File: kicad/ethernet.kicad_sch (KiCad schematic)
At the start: 83 parts, among them J1 RJ45_Abracon_ARJP11A-MASA-B-A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, J2 Conn_Coaxial, J3 JTAG, J4 USB_C_Receptacle_USB2.0, J5 Conn_Coaxial, J6 Conn_Coaxial, Q1 BSO220N03MD, SW1 KSC701, SW2 KSC701, U1 MSP432E401Y, U2 MAX-8Q, U3 TPD4S014, U4 74AUC2G34, U5 74AUC2G34, U6 MAX40200AUK, Y1 NX3225GA-25.000M-STD-CRG-2

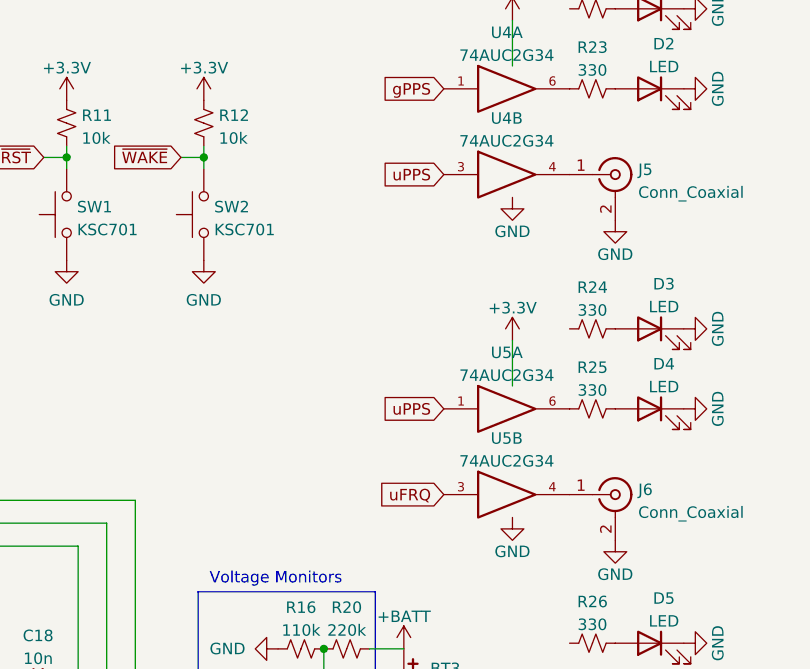
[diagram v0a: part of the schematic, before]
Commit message: update schematic
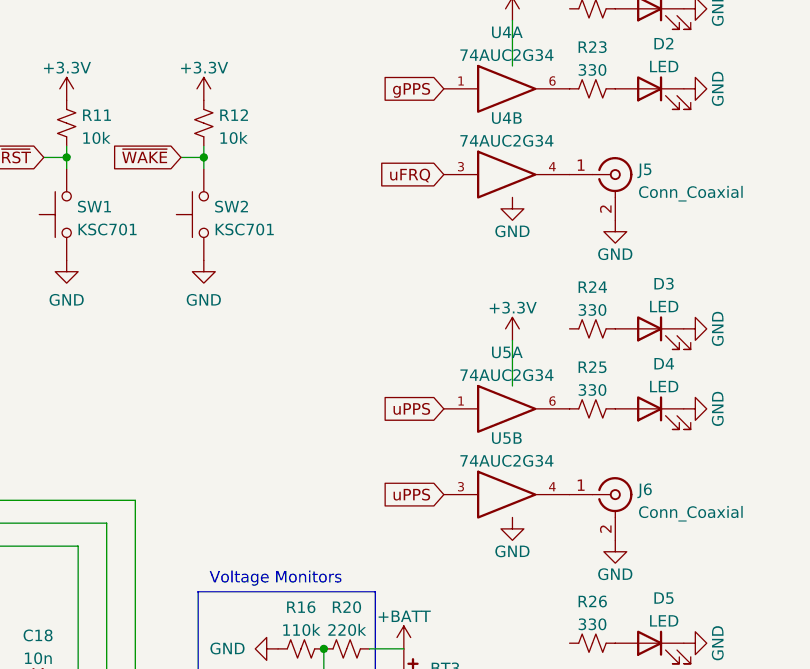
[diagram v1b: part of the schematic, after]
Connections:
- net uFRQ: now also U4.3; no longer U5.3
- net uPPS: now also U5.3; no longer U4.3
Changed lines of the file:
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@@
     )
   )
-  (global_label "uFRQ" (shape input) (at 273.05 141.605 180) (fields_autoplaced)
+  (global_label "uFRQ" (shape input) (at 273.05 106.045 180) (fields_autoplaced)
     (effects (font (size 1.27 1.27)) (justify right))
-    (property "Intersheet References" "${INTERSHEET_REFS}" (id 0) (at 265.8877 141.5256 0)
+    (property "Intersheet References" "${INTERSHEET_REFS}" (id 0) (at 265.8877 105.9656 0)
       (effects (font (size 1.27 1.27)) (justify right) hide)
     )
@@
     )
   )
-  (global_label "uPPS" (shape input) (at 273.05 106.045 180) (fields_autoplaced)
+  (global_label "uPPS" (shape input) (at 273.05 141.605 180) (fields_autoplaced)
     (effects (font (size 1.27 1.27)) (justify right))
-    (property "Intersheet References" "${INTERSHEET_REFS}" (id 0) (at 265.8272 105.9656 0)
+    (property "Intersheet References" "${INTERSHEET_REFS}" (id 0) (at 265.8272 141.5256 0)
       (effects (font (size 1.27 1.27)) (justify right) hide)
     )

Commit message: board layout progress
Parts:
- removed D7, D8: MBR0520L, Diode_SMD:D_SOD-123, symbol Device:D_Schottky
- removed J4: USB_C_Receptacle_USB2.0, Connector_USB:USB_C_Receptacle_XKB_U262-16XN-4BVC11, symbol Connector:USB_C_Receptacle_USB2.0
- removed L2: LSXBH8080YKL101M, symbol Device:L_Small
- removed Q1: BSO220N03MD, Package_SO:SOIC-8_3.9x4.9mm_P1.27mm, symbol Device:Q_Dual_NMOS_S1G1S2G2D2D2D1D1
- removed R18: 110k, Resistor_SMD:R_0805_2012Metric, symbol Device:R_Small_US
- removed R21, R22: 220k, Resistor_SMD:R_0805_2012Metric, symbol Device:R_Small_US
- removed R28, R29: 10k, Resistor_SMD:R_0805_2012Metric, symbol Device:R_Small_US
- removed SW2: KSC701, Button_Switch_SMD:SW_Push_1P1T_NO_CK_KSC7xxJ, symbol Switch:SW_Push
- removed U3: TPD4S014, Package_SON:Texas_S-PWSON-N10, symbol Power_Protection:TPD4S014
- removed U6: MAX40200AUK, Package_TO_SOT_SMD:SOT-23-5, symbol Analog_Switch:MAX40200AUK
- added BT4: NiMH, Battery:BatteryHolder_Keystone_2466_1xAAA, symbol Device:Battery_Cell
- added C25: 100n, Capacitor_SMD:C_0805_2012Metric, symbol Device:C_Small
- added D7: HSMW-C170, LED_SMD:LED_0805_2012Metric, symbol Device:LED
- added D9: RB168L100DDTE25, Diode_SMD:D_SMA, symbol Device:D_Schottky
- added Q1, Q2: 3904, Package_TO_SOT_SMD:SOT-23, symbol Device:Q_NPN_BEC
- added U3: TLV75733PDRV, Package_SON:WSON-6-1EP_2x2mm_P0.65mm_EP1x1.6mm, symbol Regulator_Linear:TLV75733PDRV
- added U6: LT1634BCMS8-2.5, Package_SO:MSOP-8_3x3mm_P0.65mm, symbol Reference_Voltage:LT1634BCMS8-2.5
- added U7: 4N25, Package_DIP:SMDIP-6_W9.53mm, symbol Isolator:4N25
- C19: value 10n -> 100n
- C20: value 10n -> 10u
- C3: value 100n -> 10u
- R12: value 10k -> 3k
- R15: value 5.1k -> 1k
- R17: value 110k -> 2.5k
- R6: value 49.9 -> 1k
- R7: value 5.1k -> 2.5k
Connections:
- net +5VP is gone; now on net +BATT: C22.2, C23.2
- net +3V3: now also C19.2, C3.2, U1.11 (PQ2), U1.116 (PJ0), U1.117 (PJ1), U1.118 (PP0), U1.119 (PP1), U1.12 (PE3), U1.120 (PB5), U1.121 (PB4), U1.123 (PE4), U1.124 (PE5), U1.125 (PD4), U1.126 (PD5), U1.128 (PD7), U1.13 (PE2), U1.18 (PK0), U1.19 (PK1), U1.2 (PD1), U1.20 (PK2), U1.21 (PK3), U1.22 (PC7), U1.23 (PC6), U1.24 (PC5), U1.25 (PC4), U1.27 (PQ3), U1.3 (PD2), U1.4 (PD3), U1.5 (PQ0), U1.6 (PQ1), U1.71 (PM7), U1.72 (PM6), U1.73 (PM5), U1.74 (PM4), U1.95 (PB0), U1.96 (PB1), C25.1, U3.1 (OUT); no longer R12.2
- net +BATT: now also C20.2, R12.2, R7.2, BT4.1 (+), D7.2 (A), D9.1 (K), Q1.3 (C), U3.6 (IN), U7.1; no longer BT3.1 (+)
- net GND: now also C3.1, R15.1, R17.1, R6.1, TR1.2, U1.64 (~{WAKE}), U1.66 (XOSC0), C25.2, U3.3 (GND), U3.7 (GND), U6.4 (A); no longer C3.2, R15.2, R17.2, R7.2, TR1.5
- net -POE: now reaches J1.10 (V-)
- net -POE: now also C24.1
- net +POE: now reaches J1.9 (V+)
- net +POE: now also C24.2
- net at C21.2: no longer C24.2
- net at TR1.1: now also D9.2 (A)
- net PLL_LED: now reaches R24.2
- net PLL_LED: now also U1.29 (PH0)
- net at R26.2: now also U1.14 (PE1)
- net at C18.2, R16.1, R20.2: now also U1.1 (PD0); no longer U1.14 (PE1)
- net at U1.15 (PE0): now also R27.2
- net GPS_LED: now reaches U1.30 (PH1)
- net GPS_LED: now also R19.2
- net at R7.1: now also Q1.1 (B), U6.6 (K)
- net at R6.2: now also D7.1 (K), U3.4 (EN)
- net D+: no longer names the net of U1.94 (PL6)
- net D-: no longer names the net of U1.93 (PL7)
- net ~{WAKE}: no longer names the net of R12.1
- net ~{WAKE}: now also R17.2, Q2.1 (B); no longer U1.64 (~{WAKE})
- new net: Q1.2 (E), Q2.2 (E), R15.2
- new net: Q2.3 (C), U7.2
- new net: BT3.1 (+), BT4.2 (-)
- now unconnected: C21.1
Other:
- note removed: "Voltage Monitors"
- moved on the sheet: BT1, BT2, BT3, C18, C21, C22, C23, C24, D5, D6, R16, R20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

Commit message: board layout update
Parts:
- removed BT1, BT2, BT3, BT4: NiMH, Battery:BatteryHolder_Keystone_2466_1xAAA, symbol Device:Battery_Cell
- added C26: 10u, Capacitor_SMD:C_0805_2012Metric, symbol Device:C_Small
- added C27: 1n, Capacitor_SMD:C_0805_2012Metric, symbol Device:C_Small
- added C?: 100n, Capacitor_SMD:C_0805_2012Metric, symbol Device:C_Small
- added J4: BATT, Connector_PinHeader_2.54mm:PinHeader_1x02_P2.54mm_Vertical, symbol Connector:Conn_01x02_Male
- added J7: POE, Connector_PinHeader_2.54mm:PinHeader_1x02_P2.54mm_Vertical, symbol Connector:Conn_01x02_Male
- added Q3: BSC340N08NS3G, Package_TO_SOT_SMD:TDSON-8-1, symbol Transistor_FET:BSC340N08NS3G
- added Q4: MMBT5401L, Package_TO_SOT_SMD:SOT-23, symbol Device:Q_PNP_BEC
- added Q? (x5): 3904, Package_TO_SOT_SMD:SOT-23, symbol Device:Q_NPN_BEC
- added Q? (x2): 3906, Package_TO_SOT_SMD:SOT-23, symbol Device:Q_PNP_BEC
- added R18: 750m, Resistor_SMD:R_1206_3216Metric, symbol Device:R_Small_US
- added R21: 4.7k, Resistor_SMD:R_0805_2012Metric, symbol Device:R_Small_US
- added R? (x2): 1k, Resistor_SMD:R_0805_2012Metric, symbol Device:R_Small_US
- added R? (x2): 150k, Resistor_SMD:R_0805_2012Metric, symbol Device:R_Small_US
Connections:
- net +BATT: now also C21.1, C26.1, J4.1 (Pin_1)
- net +POE: now also TR1.6, Q4.2 (E), Q?.3 (C), R?.2; no longer C24.2, J1.9 (V+)
- net -POE: now also C27.1, C?.1, Q?.2 (E), Q?.2 (E), Q?.2 (E), Q?.3 (C), R18.1, R?.2; no longer C24.1, J1.10 (V-)
- net GND: now also C21.2, C26.2, J4.2 (Pin_2)
- net at TR1.1: no longer D9.2 (A)
- net at TR1.3: now also D9.2 (A)
- net PSW: now reaches TR1.4
- net PSW: now also Q3.5 (D), R21.2
- new net: C24.1, J1.10 (V-), J7.1 (Pin_1)
- new net: C24.2, J1.9 (V+), J7.2 (Pin_2)
- new net: Q?.1 (B), Q?.3 (C)
- new net: Q?.3 (C), R?.1
- new net: Q?.1 (B), R?.1, R?.1
- new net: Q?.1 (B), Q?.1 (B), Q?.3 (C), Q?.3 (C)
- new net: Q3.4 (G), Q?.2 (E), Q?.2 (E)
- new net: C?.2, Q?.2 (E), Q?.2 (E), Q?.3 (C)
- new net: Q4.1 (B), R21.1
- new net: Q?.1 (B), R?.2 (x2)
- new net: Q?.1 (B), R?.1
- new net ISENSE: C27.2, Q3.1 (S), Q3.2 (S), Q3.3 (S), R18.2
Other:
- moved on the sheet: C21, TR1

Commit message: finishing board layout
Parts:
- added C29, C30: 10u, Capacitor_SMD:C_0805_2012Metric, symbol Device:C_Small
- added C31: 100n, Capacitor_SMD:C_0805_2012Metric, symbol Device:C_Small
- added D8: BZX84C12VLY, Diode_SMD:D_SOT-23_ANK, symbol Diode:BZX84Cxx
- added J8: POE+, Connector_Pin:Pin_D0.9mm_L10.0mm_W2.4mm_FlatFork, symbol Connector:Conn_01x01_Male
- added J9: POE-, Connector_Pin:Pin_D0.9mm_L10.0mm_W2.4mm_FlatFork, symbol Connector:Conn_01x01_Male
- added Q12: 3906, Package_TO_SOT_SMD:SOT-23, symbol Device:Q_PNP_BEC
- added Q13: 3904, Package_TO_SOT_SMD:SOT-23, symbol Device:Q_NPN_BEC
- added R31: 100, Resistor_SMD:R_0805_2012Metric, symbol Device:R_Small_US
- added R32, R33, R34: 10k, Resistor_SMD:R_0805_2012Metric, symbol Device:R_Small_US
- gave numbers to parts that had none: 12
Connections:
- net +POE: now also C29.1, C30.1, J8.1 (Pin_1)
- net -POE: now also U7.4, C29.2, C30.2, C31.1, J9.1 (Pin_1), Q13.2 (E)
- net ISENSE: now also R31.2
- net at Q10.1 (B), Q11.3 (C): now also D8.2 (A)
- net at Q9.1 (B), R29.1, R30.1: now also Q4.3 (C), R34.2
- net VDRV: now reaches C28.2, Q5.3 (C), Q7.2 (E), Q8.2 (E)
- net VDRV: now also C31.2, Q12.2 (E), R32.2
- net at U7.5: now also Q12.1 (B), R32.1, R33.2
- net at Q7.1 (B), R22.1: now also D8.1 (K)
- new net: Q13.3 (C), R33.1
- new net: Q12.3 (C), R34.1
- new net: Q13.1 (B), R31.1

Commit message: board layout update
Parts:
- added C32: 10u, Capacitor_SMD:C_0805_2012Metric, symbol Device:C_Small
- added C33, C34: 100n, Capacitor_SMD:C_0805_2012Metric, symbol Device:C_Small
- C29, C30: footprint Capacitor_SMD:C_0805_2012Metric -> Capacitor_SMD:C_1210_3225Metric
- D9: value RB168L100DDTE25 -> RB068L100TE25
- R21: value 4.7k -> 10k
- R31: value 100 -> 330
- R34: value 10k -> 3k
- R7: value 2.5k -> 3k
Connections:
- net +3V3: now also C32.1, C33.1, C34.1
- net +BATT: now also R12.1; no longer R12.2
- net GND: now also C32.2, C33.2, C34.2
- net at Q2.1 (B), R17.2: now also R12.2; no longer R12.1
- net at Q4.3 (C), Q9.1 (B), R29.1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: now also R34.1; no longer R34.2
- net RECT: now reaches D9.2 (A), TR1.3
- net at Q12.3 (C): now also R34.2; no longer R34.1
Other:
- moved on the sheet: R12, R17, R34

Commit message: board layout update
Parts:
- added C35: 100n, Capacitor_SMD:C_0805_2012Metric, symbol Device:C_Small
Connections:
- net +3V3: now also C35.1
- net GND: now also C35.2
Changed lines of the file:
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@@
     (pin "1")
+  )
+  (symbol (lib_id "Device:C_Small") (at 327.66 52.07 0) (unit 1)
+    (in_bom yes) (on_board yes) (fields_autoplaced)
+    (property "Reference" "C35" (id 0) (at 329.9841 51.2416 0)
+      (effects (font (size 1.27 1.27)) (justify left))
+    )
+    (property "Value" "100n" (id 1) (at 329.9841 53.7785 0)
+      (effects (font (size 1.27 1.27)) (justify left))
+    )
+    (property "Footprint" "Capacitor_SMD:C_0805_2012Metric" (id 2) (at 327.66 52.07 0)
+      (effects (font (size 1.27 1.27)) hide)
+    )
+    (property "Datasheet" "~" (id 3) (at 327.66 52.07 0)
+      (effects (font (size 1.27 1.27)) hide)
+    )
+    (pin "1")
+    (pin "2")
   )
   (symbol (lib_id "Device:C_Small") (at 265.43 187.96 0) (unit 1)
@@
     (pin "1")
   )
+  (symbol (lib_id "power:GND") (at 327.66 54.61 0) (unit 1)
+    (in_bom yes) (on_board yes) (fields_autoplaced)
+    (property "Reference" "#PWR0197" (id 0) (at 327.66 60.96 0)
+      (effects (font (size 1.27 1.27)) hide)
+    )
+    (property "Value" "GND" (id 1) (at 327.66 59.0534 0))
+    (property "Footprint" "" (id 2) (at 327.66 54.61 0)
+      (effects (font (size 1.27 1.27)) hide)
+    )
+    (property "Datasheet" "" (id 3) (at 327.66 54.61 0)
+      (effects (font (size 1.27 1.27)) hide)
+    )
+    (pin "1")
+  )
   (symbol (lib_id "Device:R_Small_US") (at 353.695 221.615 270) (unit 1)
     (in_bom yes) (on_board yes) (fields_autoplaced)
@@
     (pin "2")
   )
+  (symbol (lib_id "power:+3.3V") (at 327.66 49.53 0) (unit 1)
+    (in_bom yes) (on_board yes)
+    (property "Reference" "#PWR0196" (id 0) (at 327.66 53.34 0)
+      (effects (font (size 1.27 1.27)) hide)
+    )
+    (property "Value" "+3.3V" (id 1) (at 327.66 45.9542 0))
+    (property "Footprint" "" (id 2) (at 327.66 49.53 0)
+      (effects (font (size 1.27 1.27)) hide)
+    )
+    (property "Datasheet" "" (id 3) (at 327.66 49.53 0)
+      (effects (font (size 1.27 1.27)) hide)
+    )
+    (pin "1")
+  )
   (symbol (lib_id "power:+3.3V") (at 336.55 31.75 0) (unit 1)
     (in_bom yes) (on_board yes)
@@
       (reference "#PWR0195") (unit 1) (value "+3.3V") (footprint "")
     )
+    (path "/b794d5f3-bb58-4a83-b180-e930ca706cb4"
+      (reference "#PWR0196") (unit 1) (value "+3.3V") (footprint "")
+    )
+    (path "/7c665576-1ee3-4572-ace4-c518413c36cf"
+      (reference "#PWR0197") (unit 1) (value "GND") (footprint "")
+    )
     (path "/61236a36-6ce0-4537-a076-8a3910347465"
       (reference "C1") (unit 1) (value "12p") (footprint "Capacitor_SMD:C_0805_2012Metric")
@@
       (reference "C34") (unit 1) (value "100n") (footprint "Capacitor_SMD:C_0805_2012Metric")
     )
+    (path "/391996cc-7a55-441b-aab0-6064482b5410"
+      (reference "C35") (unit 1) (value "100n") (footprint "Capacitor_SMD:C_0805_2012Metric")
+    )
     (path "/a3d61d57-ecb8-4521-9622-3daabfc881cd"

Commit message: update schematic
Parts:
- removed U6: LT1634BCMS8-2.5, Package_SO:MSOP-8_3x3mm_P0.65mm, symbol Reference_Voltage:LT1634BCMS8-2.5
- added U6: LM4040DBZ-2.5, Package_TO_SOT_SMD:SOT-23, symbol Reference_Voltage:LM4040DBZ-2.5
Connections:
- net GND: now also U6.2 (A)
- net at Q1.1 (B), R7.1: now also U6.1 (K)
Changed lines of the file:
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@@
   (junction (at 375.92 204.47) (diameter 0) (color 0 0 0 0)
   )
-  (junction (at 266.7 228.6) (diameter 0) (color 0 0 0 0)
-  )
   (junction (at 217.17 198.12) (diameter 0) (color 0 0 0 0)
   )
@@
   (junction (at 279.4 62.23) (diameter 0) (color 0 0 0 0)
   )
+  (junction (at 266.7 228.6) (diameter 0) (color 0 0 0 0)
+  )
   (junction (at 66.675 68.58) (diameter 0) (color 0 0 0 0)
   )
@@
     (pin "2")
   )
+  (symbol (lib_id "Reference_Voltage:LM4040DBZ-2.5") (at 266.7 232.41 90) (unit 1)
+    (in_bom yes) (on_board yes)
+    (property "Reference" "U6" (id 0) (at 264.16 231.14 90)
+      (effects (font (size 1.27 1.27)) (justify left))
+    )
+    (property "Value" "LM4040DBZ-2.5" (id 1) (at 264.16 233.68 90)
+      (effects (font (size 1.27 1.27)) (justify left))
+    )
+    (property "Footprint" "Package_TO_SOT_SMD:SOT-23" (id 2) (at 271.78 232.41 0)
+      (effects (font (size 1.27 1.27) italic) hide)
+    )
+    (property "Datasheet" "http://www.ti.com/lit/ds/symlink/lm4040-n.pdf" (id 3) (at 266.7 232.41 0)
+      (effects (font (size 1.27 1.27) italic) hide)
+    )
+    (pin "1")
+    (pin "2")
+  )
   (symbol (lib_id "Device:R_Small_US") (at 265.43 208.28 180) (unit 1)
     (in_bom yes) (on_board yes) (fields_autoplaced)
@@
     (pin "1")
   )
-  (symbol (lib_id "Reference_Voltage:LT1634BCMS8-2.5") (at 266.7 232.41 270) (mirror x) (unit 1)
-    (in_bom yes) (on_board yes) (fields_autoplaced)
-    (property "Reference" "U6" (id 0) (at 264.6935 231.5753 90)
-      (effects (font (size 1.27 1.27)) (justify right))
-    )
-    (property "Value" "LT1634BCMS8-2.5" (id 1) (at 264.6935 234.1122 90)
-      (effects (font (size 1.27 1.27)) (justify right))
-    )
-    (property "Footprint" "Package_SO:MSOP-8_3x3mm_P0.65mm" (id 2) (at 261.62 232.41 0)
-      (effects (font (size 1.27 1.27)) hide)
-    )
-    (property "Datasheet" "https://www.analog.com/media/en/technical-documentation/data-sheets/1634ff.pdf" (id 3) (at 266.7 232.41 0)
-      (effects (font (size 1.27 1.27)) hide)
-    )
-    (pin "4")
-    (pin "5")
-    (pin "6")
-  )
   (symbol (lib_id "power:+3.3V") (at 96.52 38.1 90) (unit 1)
     (in_bom yes) (on_board yes)
@@
       (reference "U5") (unit 2) (value "74AUC2G34") (footprint "Package_TO_SOT_SMD:SOT-23-6")
     )
-    (path "/b47eff88-4503-45f2-b0e0-3ff9f402786f"
-      (reference "U6") (unit 1) (value "LT1634BCMS8-2.5") (footprint "Package_SO:MSOP-8_3x3mm_P0.65mm")
+    (path "/a535654f-aea5-43c9-9ab8-783ef20dcacc"
+      (reference "U6") (unit 1) (value "LM4040DBZ-2.5") (footprint "Package_TO_SOT_SMD:SOT-23")
     )
     (path "/1a8a1d0e-2edf-4bbf-b630-1de1b00f00ef"
